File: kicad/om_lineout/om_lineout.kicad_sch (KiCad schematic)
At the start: 49 parts, among them J1 AudioJack3, J2 AudioJack3, U1 Opamp_Quad, U2 Opamp_Quad

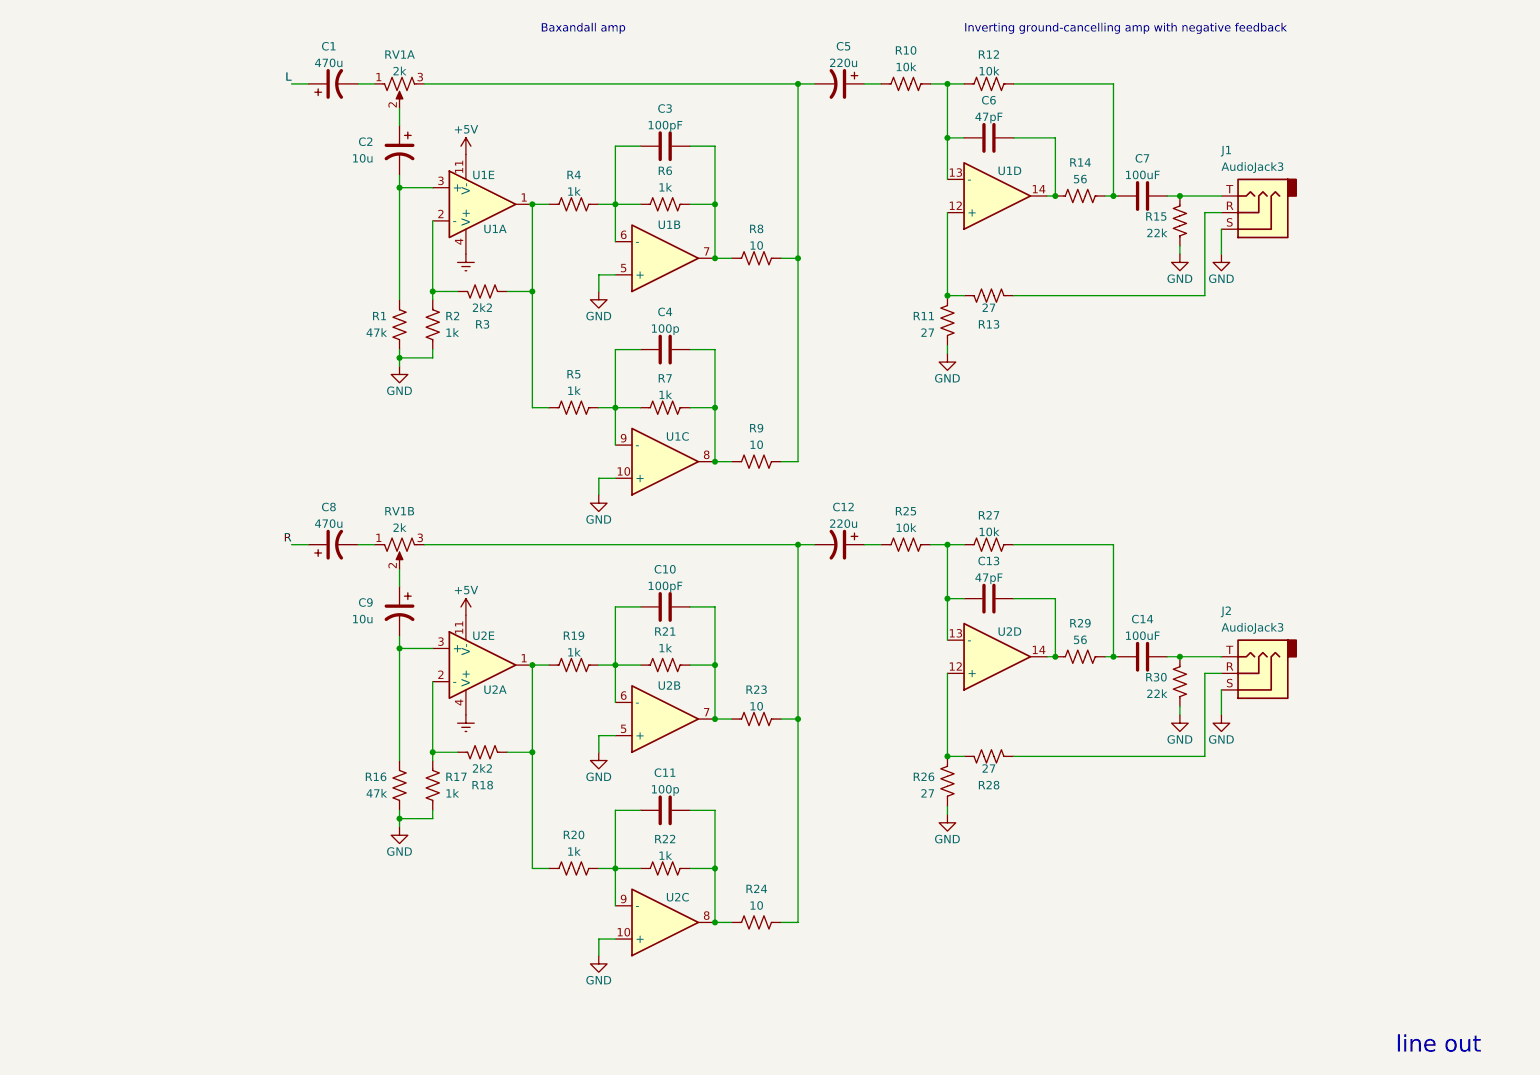
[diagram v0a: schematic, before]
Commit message: line output gain staging
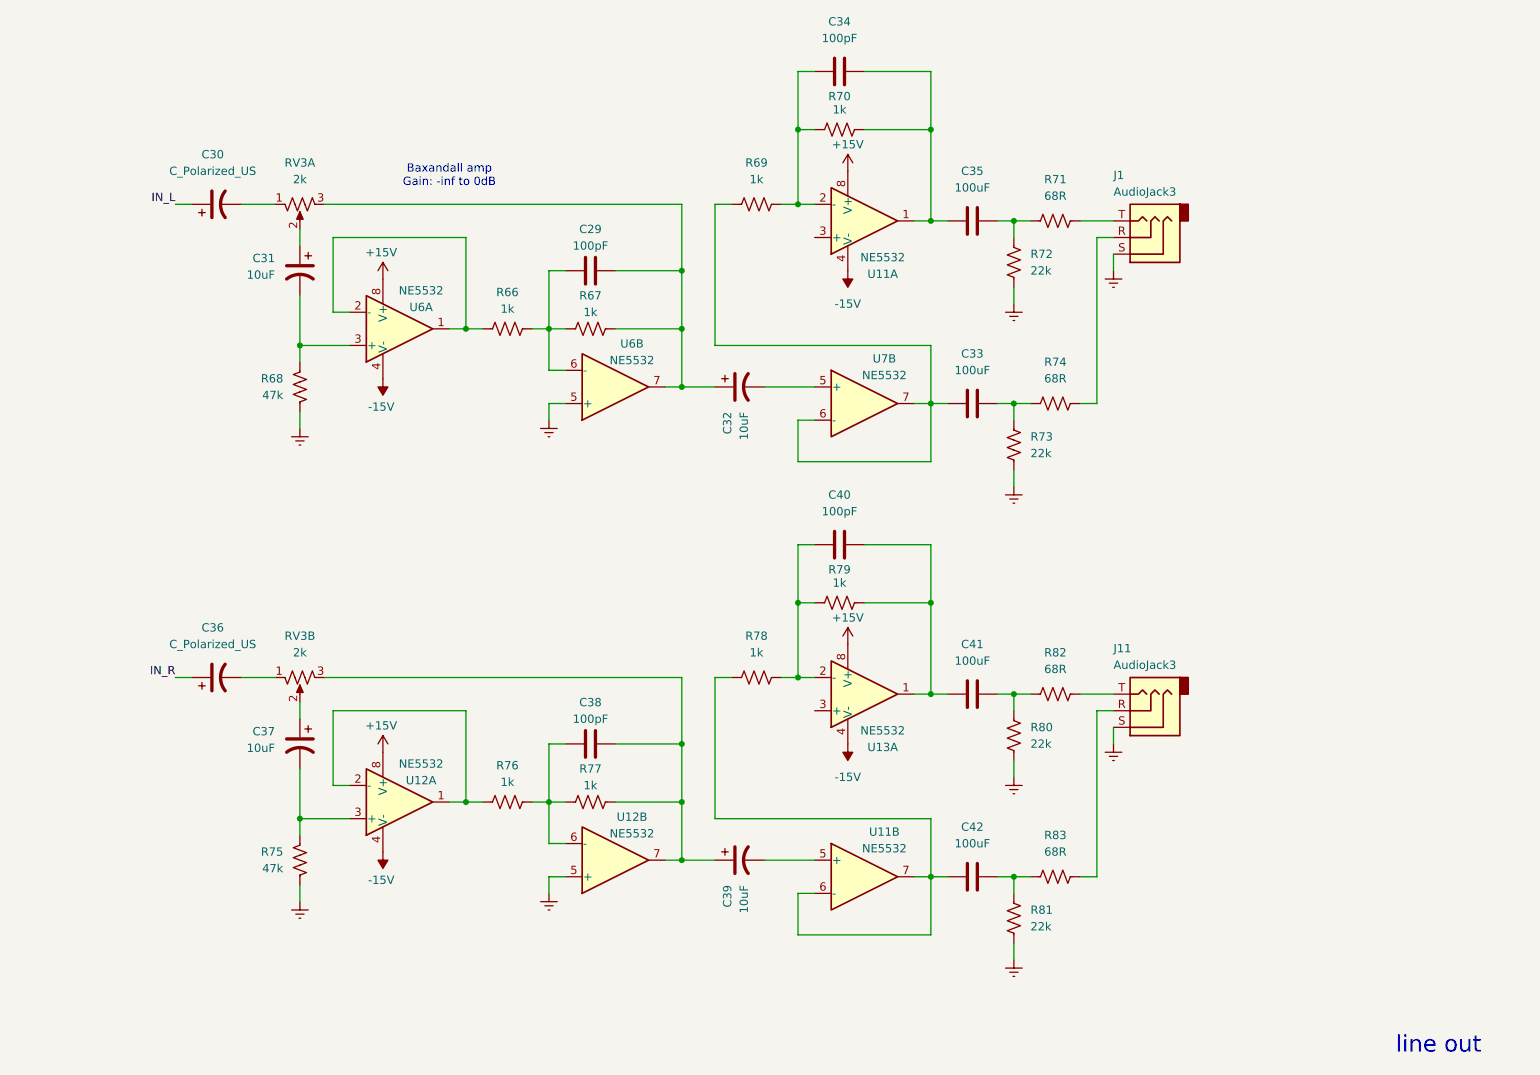
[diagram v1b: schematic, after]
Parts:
- removed C1, C8: 470u, symbol Device:C_Polarized_US
- removed C10, C3: 100pF, symbol Device:C
- removed C11, C4: 100p, symbol Device:C
- removed C12, C5: 220u, symbol Device:C_Polarized_US
- removed C13, C6: 47pF, symbol Device:C
- removed C14, C7: 100uF, symbol Device:C
- removed C2, C9: 10u, symbol Device:C_Polarized_US
- removed J2: AudioJack3, symbol Connector_Audio:AudioJack3
- removed R1, R16: 47k, symbol Device:R_US
- removed R10, R12, R25, R27: 10k, symbol Device:R_US
- removed R11, R13, R26, R28: 27, symbol Device:R_US
- removed R14, R29: 56, symbol Device:R_US
- removed R15, R30: 22k, symbol Device:R_US
- removed R17, R19, R2, R20, R21, R22, R4, R5, R6, R7: 1k, symbol Device:R_US
- removed R18, R3: 2k2, symbol Device:R_US
- removed R23, R24, R8, R9: 10, symbol Device:R_US
- removed RV1: 2k, symbol openmic:R_Potentiometer_US_Dual
- removed U1, U2: Opamp_Quad, symbol Device:Opamp_Quad
- added C29, C34, C38, C40: 100pF, symbol Device:C
- added C30, C36: C_Polarized_US, symbol Device:C_Polarized_US
- added C31, C32, C37, C39: 10uF, symbol Device:C_Polarized_US
- added C33, C35, C41, C42: 100uF, symbol Device:C
- added J11: AudioJack3, symbol Connector_Audio:AudioJack3
- added R66, R67, R69, R70, R76, R77, R78, R79: 1k, symbol Device:R_US
- added R68, R75: 47k, symbol Device:R_US
- added R71, R74, R82, R83: 68R, symbol Device:R_US
- added R72, R73, R80, R81: 22k, symbol Device:R_US
- added RV3: 2k, symbol openmic:R_Potentiometer_US_Dual
- added U11, U12, U13, U6, U7: NE5532, symbol Amplifier_Operational:NE5532
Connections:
- net GND is gone; now on net Earth: J1.S
- net Earth: now also J11.S, R68.1, R72.1, R73.1, R75.1, R80.1, R81.1, U12.5 (+), U6.5 (+)
- net at J1.T: now also R71.2
- net at J1.R: now also R74.2
- new net: C36.2, RV3.1
- new net: R66.1, U6.1, U6.2 (-)
- new net: C31.2, R68.2, U6.3 (+)
- new net: C37.1, RV3.2
- new net: C38.2, C39.1, R77.2, RV3.3, U12.7
- new net: C35.2, R71.1, R72.2
- new net: C38.1, R76.2, R77.1, U12.6 (-)
- new net: C40.2, C41.1, R79.2, U13.1
- new net: C41.2, R80.2, R82.1
- new net: C29.1, R66.2, R67.1, U6.6 (-)
- new net: C29.2, C32.1, R67.2, RV3.3, U6.7
- new net: J11.T, R82.2
- new net: C40.1, R78.2, R79.1, U13.2 (-)
- new net: C30.2, RV3.1
- new net: R76.1, U12.1, U12.2 (-)
- new net: C33.2, R73.2, R74.1
- new net: C42.1, R78.1, U11.6 (-), U11.7
- new net: C33.1, R69.1, U7.6 (-), U7.7
- new net: C34.1, R69.2, R70.1, U11.2 (-)
- new net: C32.2, U7.5 (+)
- new net: C34.2, C35.1, R70.2, U11.1
- new net: J11.R, R83.2
- new net: C42.2, R81.2, R83.1
- new net: C39.2, U11.5 (+)
- new net: C31.1, RV3.2
- new net: C37.2, R75.2, U12.3 (+)
- new net +15V: U11.8 (V+), U12.8 (V+), U13.8 (V+), U6.8 (V+)
- new net -15V: U11.4 (V-), U12.4 (V-), U13.4 (V-), U6.4 (V-)
- new net IN_L: C30.1
- new net IN_R: C36.1
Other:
- note added: "Baxandall amp Gain: -inf to 0dB"
- note removed: "Baxandall amp"
- note removed: "Inverting ground-cancelling amp with negative feedback"
- moved on the sheet: J1

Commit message: line out connections
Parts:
- added J19: Conn_01x05_Pin, symbol Connector:Conn_01x05_Pin
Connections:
- net +15V: now also J19.1 (Pin_1)
- net -15V: now also J19.2 (Pin_2)
- net Earth: now also J19.3 (Pin_3)
- net IN_L: now also J19.4 (Pin_4)
- net IN_R: now also J19.5 (Pin_5)

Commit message: headphone driver (#7)
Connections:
- net Earth: now also U11.3 (+), U13.3 (+)
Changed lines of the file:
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@@
+	(wire
+		(pts
+			(xy 133.35 123.19) (xy 135.89 123.19)
+		)
+		(stroke
+			(width 0)
+			(type default)
+		)
+	)
 	(wire
 		(pts
@@
 	(wire
 		(pts
+			(xy 133.35 125.73) (xy 133.35 123.19)
+		)
+		(stroke
+			(width 0)
+			(type default)
+		)
+	)
+	(wire
+		(pts
 			(xy 26.67 80.01) (xy 34.29 80.01)
 		)
@@
 		(pts
 			(xy 57.15 69.85) (xy 57.15 67.31)
+		)
+		(stroke
+			(width 0)
+			(type default)
+		)
+	)
+	(wire
+		(pts
+			(xy 133.35 50.8) (xy 135.89 50.8)
+		)
+		(stroke
+			(width 0)
+			(type default)
+		)
+	)
+	(wire
+		(pts
+			(xy 133.35 53.34) (xy 133.35 50.8)
 		)
 		(stroke
@@
 				(path "/c6024129-74a6-4977-a9ee-12cbe1bccdc5/5bda4d1a-0137-4b23-b9d9-89a821d3e2d9"
 					(reference "#PWR086")
+					(unit 1)
+				)
+			)
+		)
+	)
+	(symbol
+		(lib_id "power:Earth")
+		(at 133.35 53.34 0)
+		(unit 1)
+		(exclude_from_sim no)
+		(in_bom yes)
+		(on_board yes)
+		(dnp no)
+		(fields_autoplaced yes)
+		(property "Reference" "#PWR0104"
+			(at 133.35 59.69 0)
+			(effects
+				(font
+					(size 1.27 1.27)
+				)
+				(hide yes)
+			)
+		)
+		(property "Value" "Earth"
+			(at 133.35 58.42 0)
+			(effects
+				(font
+					(size 1.27 1.27)
+				)
+				(hide yes)
+			)
+		)
+		(property "Footprint" ""
+			(at 133.35 53.34 0)
+			(effects
+				(font
+					(size 1.27 1.27)
+				)
+				(hide yes)
+			)
+		)
+		(property "Datasheet" "~"
+			(at 133.35 53.34 0)
+			(effects
+				(font
+					(size 1.27 1.27)
+				)
+				(hide yes)
+			)
+		)
+		(property "Description" "Power symbol creates a global label with name \"Earth\""
+			(at 133.35 53.34 0)
+			(effects
+				(font
+					(size 1.27 1.27)
+				)
+				(hide yes)
+			)
+		)
+		(pin "1"
+		)
+		(instances
+			(project "structure"
+				(path "/c6024129-74a6-4977-a9ee-12cbe1bccdc5/5bda4d1a-0137-4b23-b9d9-89a821d3e2d9"
+					(reference "#PWR0104")
 					(unit 1)
 				)
@@
 					(unit 1)
 				)
+			)
+		)
+	)
+	(symbol
+		(lib_id "power:Earth")
+		(at 133.35 125.73 0)
+		(unit 1)
+		(exclude_from_sim no)
+		(in_bom yes)
+		(on_board yes)
+		(dnp no)
+		(fields_autoplaced yes)
+		(property "Reference" "#PWR0105"
+			(at 133.35 132.08 0)
+			(effects
+				(font
+					(size 1.27 1.27)
+				)
+				(hide yes)
+			)
+		)
+		(property "Value" "Earth"
+			(at 133.35 130.81 0)
+			(effects
+				(font
+					(size 1.27 1.27)
+				)
+				(hide yes)
+			)
+		)
+		(property "Footprint" ""
+			(at 133.35 125.73 0)
+			(effects
+				(font
+					(size 1.27 1.27)
+				)
+				(hide yes)
+			)
+		)
+		(property "Datasheet" "~"
+			(at 133.35 125.73 0)
+			(effects
+				(font
+					(size 1.27 1.27)
+				)
+				(hide yes)
+			)
+		)
+		(property "Description" "Power symbol creates a global label with name \"Earth\""
+			(at 133.35 125.73 0)
+			(effects
+				(font
+					(size 1.27 1.27)
+				)
+				(hide yes)
+			)
+		)
+		(pin "1"
+		)
+		(instances
+			(project "structure"
+				(path "/c6024129-74a6-4977-a9ee-12cbe1bccdc5/5bda4d1a-0137-4b23-b9d9-89a821d3e2d9"
+					(reference "#PWR0105")
+					(unit 1)
+				)
